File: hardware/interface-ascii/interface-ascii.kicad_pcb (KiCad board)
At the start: 2 copper layers, 88.9 x 119.4 mm, 51 parts, among them J1 Apple 2, J2 Apple 1, J3 UART, J4 Conn_01x05, J5 ISP header, J6 Keyboard, SW1 Options, U1 ATmega328P, U2 74LS166, U3 74LS138, U4 74LS138, U5 74LS07

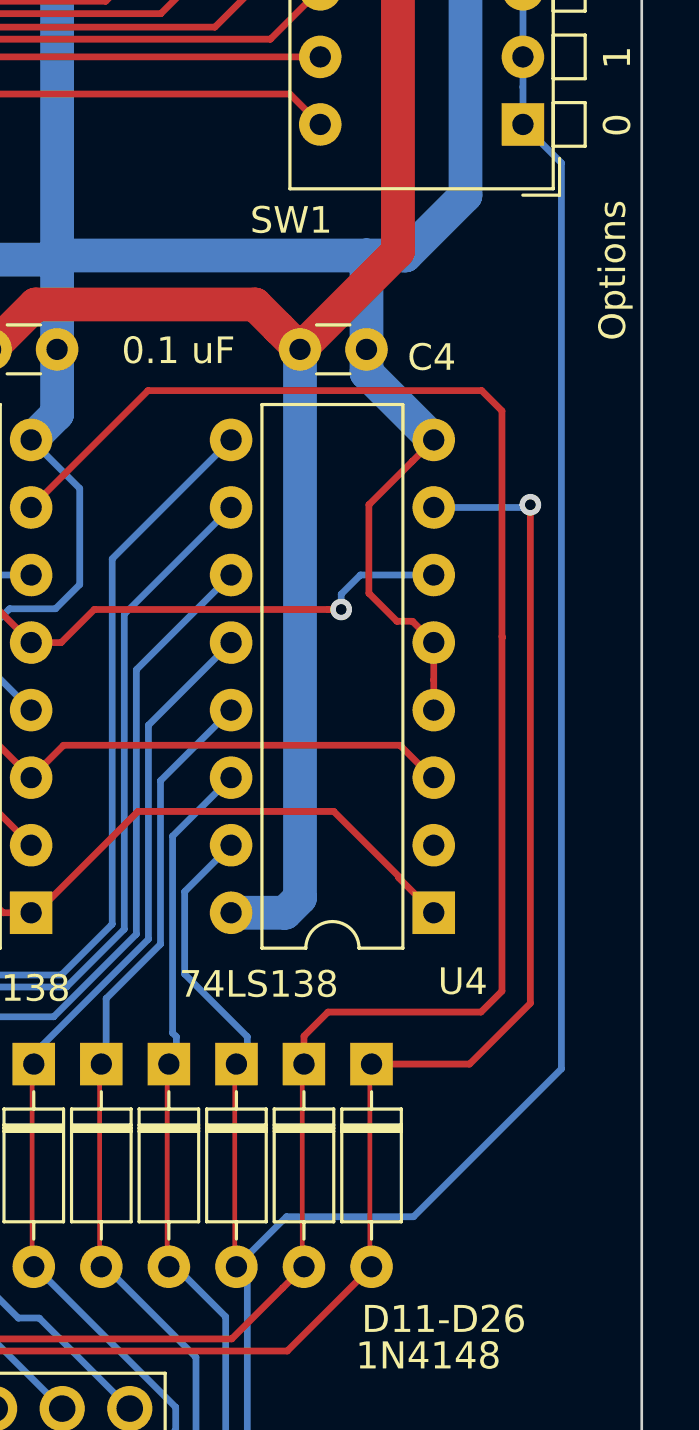
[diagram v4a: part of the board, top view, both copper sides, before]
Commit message: Move DIP switch to row 15
So keyboards with more than 8 rows can have keys on contiguous row numbers.
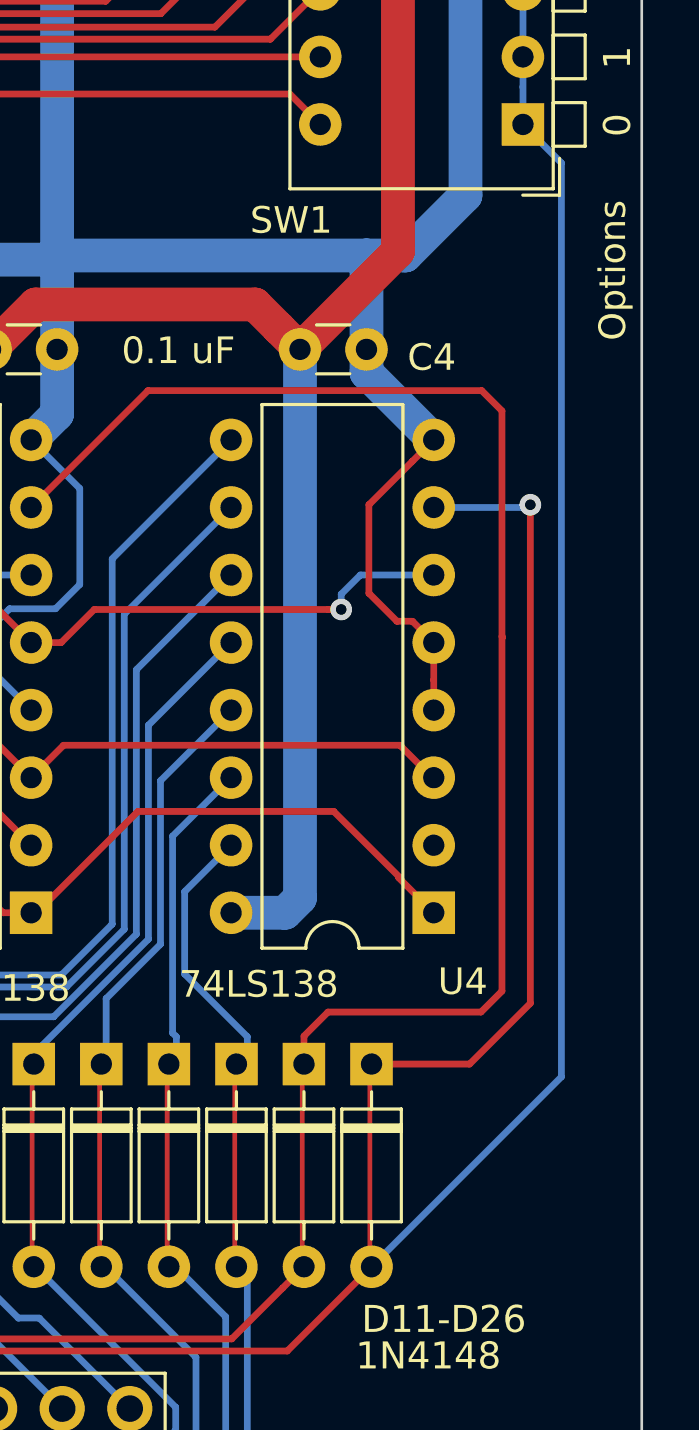
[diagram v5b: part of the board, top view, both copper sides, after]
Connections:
- SW1 pad 1: /Row8 -> /Row15
- SW1 pad 2: /Row8 -> /Row15
- SW1 pad 3: /Row8 -> /Row15
- SW1 pad 4: /Row8 -> /Row15
- SW1 pad 5: /Row8 -> /Row15
- SW1 pad 6: /Row8 -> /Row15
- SW1 pad 7: /Row8 -> /Row15
- SW1 pad 8: /Row8 -> /Row15
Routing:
- net /Row8: track 92.5 -> 23.3 mm
- net /Row15: track 18.9 -> 83.2 mm
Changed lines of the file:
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@@
     (thickness 1.6)
     (drawings 33)
-    (tracks 962)
+    (tracks 960)
     (zones 0)
     (modules 51)
@@
     )
     (pad 1 thru_hole rect (at 0 0 180) (size 1.6 1.6) (drill 0.8) (layers *.Cu *.Mask)
-      (net 37 /Row8))
+      (net 38 /Row15))
     (pad 9 thru_hole oval (at 7.62 17.78 180) (size 1.6 1.6) (drill 0.8) (layers *.Cu *.Mask)
       (net 73 "Net-(D27-Pad1)"))
     (pad 2 thru_hole oval (at 0 2.54 180) (size 1.6 1.6) (drill 0.8) (layers *.Cu *.Mask)
-      (net 37 /Row8))
+      (net 38 /Row15))
     (pad 10 thru_hole oval (at 7.62 15.24 180) (size 1.6 1.6) (drill 0.8) (layers *.Cu *.Mask)
       (net 56 "Net-(D20-Pad1)"))
     (pad 3 thru_hole oval (at 0 5.08 180) (size 1.6 1.6) (drill 0.8) (layers *.Cu *.Mask)
-      (net 37 /Row8))
+      (net 38 /Row15))
     (pad 11 thru_hole oval (at 7.62 12.7 180) (size 1.6 1.6) (drill 0.8) (layers *.Cu *.Mask)
       (net 59 "Net-(D26-Pad1)"))
     (pad 4 thru_hole oval (at 0 7.62 180) (size 1.6 1.6) (drill 0.8) (layers *.Cu *.Mask)
-      (net 37 /Row8))
+      (net 38 /Row15))
     (pad 12 thru_hole oval (at 7.62 10.16 180) (size 1.6 1.6) (drill 0.8) (layers *.Cu *.Mask)
       (net 55 "Net-(D19-Pad1)"))
     (pad 5 thru_hole oval (at 0 10.16 180) (size 1.6 1.6) (drill 0.8) (layers *.Cu *.Mask)
-      (net 37 /Row8))
+      (net 38 /Row15))
     (pad 13 thru_hole oval (at 7.62 7.62 180) (size 1.6 1.6) (drill 0.8) (layers *.Cu *.Mask)
       (net 58 "Net-(D25-Pad1)"))
     (pad 6 thru_hole oval (at 0 12.7 180) (size 1.6 1.6) (drill 0.8) (layers *.Cu *.Mask)
-      (net 37 /Row8))
+      (net 38 /Row15))
     (pad 14 thru_hole oval (at 7.62 5.08 180) (size 1.6 1.6) (drill 0.8) (layers *.Cu *.Mask)
       (net 54 "Net-(D18-Pad1)"))
     (pad 7 thru_hole oval (at 0 15.24 180) (size 1.6 1.6) (drill 0.8) (layers *.Cu *.Mask)
-      (net 37 /Row8))
+      (net 38 /Row15))
     (pad 15 thru_hole oval (at 7.62 2.54 180) (size 1.6 1.6) (drill 0.8) (layers *.Cu *.Mask)
       (net 57 "Net-(D24-Pad1)"))
     (pad 8 thru_hole oval (at 0 17.78 180) (size 1.6 1.6) (drill 0.8) (layers *.Cu *.Mask)
-      (net 37 /Row8))
+      (net 38 /Row15))
     (pad 16 thru_hole oval (at 7.62 0 180) (size 1.6 1.6) (drill 0.8) (layers *.Cu *.Mask)
       (net 53 "Net-(D17-Pad1)"))
@@
   (segment (start 237.086 169.572) (end 237.086 176.7856) (width 0.254) (layer B.Cu) (net 36))
   (segment (start 235.2318 167.7178) (end 237.086 169.572) (width 0.254) (layer B.Cu) (net 36))
-  (segment (start 248.262 110.63237) (end 248.262 112.041) (width 0.254) (layer B.Cu) (net 37))
-  (segment (start 248.262 109.501) (end 248.262 110.63237) (width 0.254) (layer B.Cu) (net 37))
-  (segment (start 248.262 112.041) (end 248.262 114.581) (width 0.254) (layer B.Cu) (net 37))
-  (segment (start 248.262 115.71237) (end 248.262 117.121) (width 0.254) (layer B.Cu) (net 37))
-  (segment (start 248.262 114.581) (end 248.262 115.71237) (width 0.254) (layer B.Cu) (net 37))
-  (segment (start 248.262 118.25237) (end 248.262 119.661) (width 0.254) (layer B.Cu) (net 37))
-  (segment (start 248.262 117.121) (end 248.262 118.25237) (width 0.254) (layer B.Cu) (net 37))
-  (segment (start 248.262 119.661) (end 248.262 122.201) (width 0.254) (layer B.Cu) (net 37))
-  (segment (start 248.262 123.33237) (end 248.262 124.741) (width 0.254) (layer B.Cu) (net 37))
-  (segment (start 248.262 122.201) (end 248.262 123.33237) (width 0.254) (layer B.Cu) (net 37))
   (segment (start 236.47959 178.56041) (end 228.85321 178.56041) (width 0.254) (layer B.Cu) (net 37))
   (segment (start 228.85321 178.56041) (end 225.8592 175.5664) (width 0.254) (layer B.Cu) (net 37))
   (segment (start 237.8988 177.1412) (end 236.47959 178.56041) (width 0.254) (layer B.Cu) (net 37))
   (segment (start 237.8988 167.7178) (end 237.8988 177.1412) (width 0.254) (layer B.Cu) (net 37))
-  (segment (start 239.3696 165.8128) (end 237.49 167.6924) (width 0.254) (layer B.Cu) (net 37))
-  (segment (start 244.1472 165.8128) (end 239.3696 165.8128) (width 0.254) (layer B.Cu) (net 37))
-  (segment (start 249.7098 126.1888) (end 249.7098 160.2502) (width 0.254) (layer B.Cu) (net 37))
-  (segment (start 249.7098 160.2502) (end 244.1472 165.8128) (width 0.254) (layer B.Cu) (net 37))
-  (segment (start 248.262 124.741) (end 249.7098 126.1888) (width 0.254) (layer B.Cu) (net 37))
-  (segment (start 248.262 108.09237) (end 248.262 109.501) (width 0.254) (layer B.Cu) (net 37))
-  (segment (start 248.262 106.961) (end 248.262 108.09237) (width 0.254) (layer B.Cu) (net 37))
   (segment (start 242.57 167.6924) (end 239.401378 170.861022) (width 0.254) (layer F.Cu) (net 38))
   (segment (start 226.709199 172.176401) (end 225.8592 173.0264) (width 0.254) (layer F.Cu) (net 38))
   (segment (start 239.401378 170.861022) (end 228.024578 170.861022) (width 0.254) (layer F.Cu) (net 38))
   (segment (start 228.024578 170.861022) (end 226.709199 172.176401) (width 0.254) (layer F.Cu) (net 38))
+  (segment (start 248.262 106.961) (end 248.262 108.09237) (width 0.254) (layer B.Cu) (net 38))
+  (segment (start 248.262 108.09237) (end 248.262 109.501) (width 0.254) (layer B.Cu) (net 38))
+  (segment (start 248.262 122.201) (end 248.262 123.33237) (width 0.254) (layer B.Cu) (net 38))
+  (segment (start 248.262 123.33237) (end 248.262 124.741) (width 0.254) (layer B.Cu) (net 38))
+  (segment (start 248.262 119.661) (end 248.262 122.201) (width 0.254) (layer B.Cu) (net 38))
+  (segment (start 248.262 117.121) (end 248.262 118.25237) (width 0.254) (layer B.Cu) (net 38))
+  (segment (start 248.262 118.25237) (end 248.262 119.661) (width 0.254) (layer B.Cu) (net 38))
+  (segment (start 248.262 114.581) (end 248.262 115.71237) (width 0.254) (layer B.Cu) (net 38))
+  (segment (start 248.262 115.71237) (end 248.262 117.121) (width 0.254) (layer B.Cu) (net 38))
+  (segment (start 248.262 112.041) (end 248.262 114.581) (width 0.254) (layer B.Cu) (net 38))
+  (segment (start 248.262 109.501) (end 248.262 110.63237) (width 0.254) (layer B.Cu) (net 38))
+  (segment (start 248.262 110.63237) (end 248.262 112.041) (width 0.254) (layer B.Cu) (net 38))
+  (segment (start 249.7098 160.5526) (end 242.57 167.6924) (width 0.254) (layer B.Cu) (net 38))
+  (segment (start 249.7098 126.1888) (end 249.7098 160.5526) (width 0.254) (layer B.Cu) (net 38))
+  (segment (start 248.262 124.741) (end 249.7098 126.1888) (width 0.254) (layer B.Cu) (net 38))
   (segment (start 224.7416 170.2578) (end 225.6306 170.2578) (width 0.254) (layer B.Cu) (net 39))
   (segment (start 227.549201 172.176401) (end 228.3992 173.0264) (width 0.254) (layer B.Cu) (net 39))

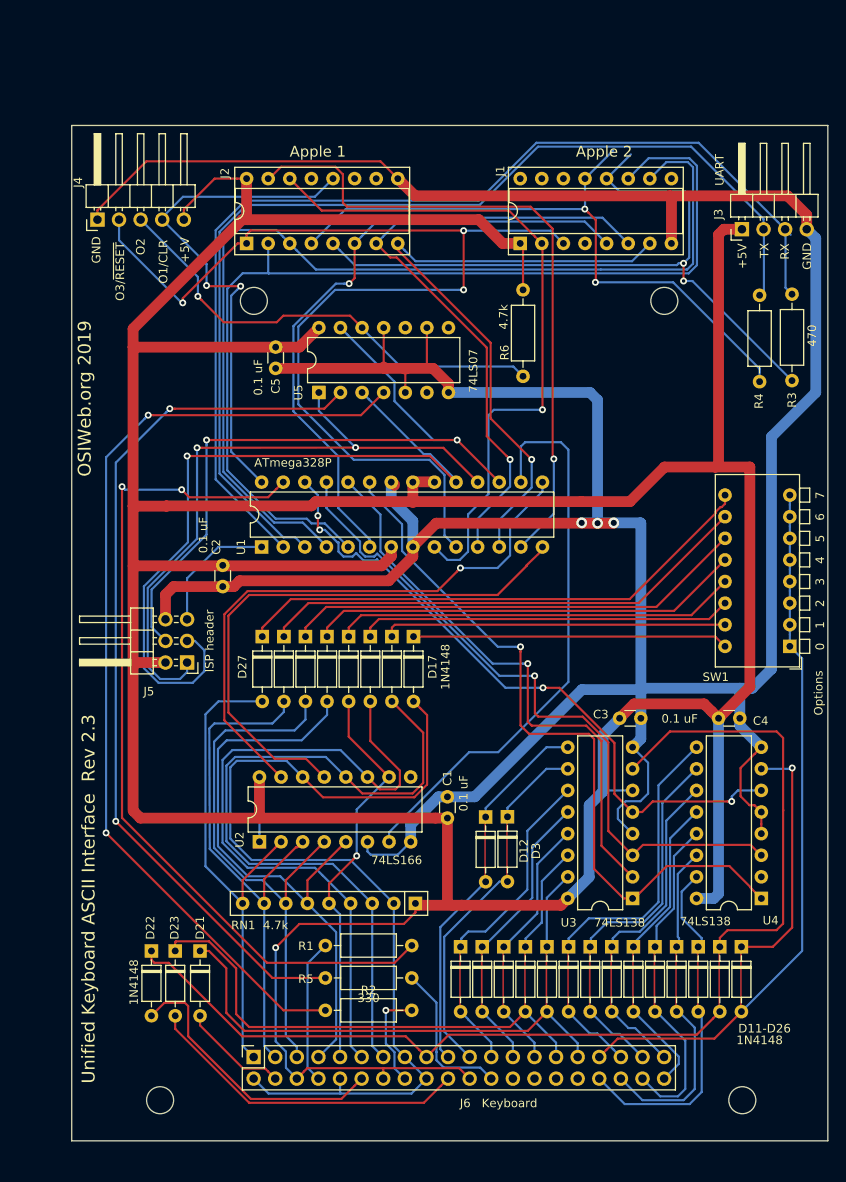
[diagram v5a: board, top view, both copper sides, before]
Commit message: Add SOL-20 connector
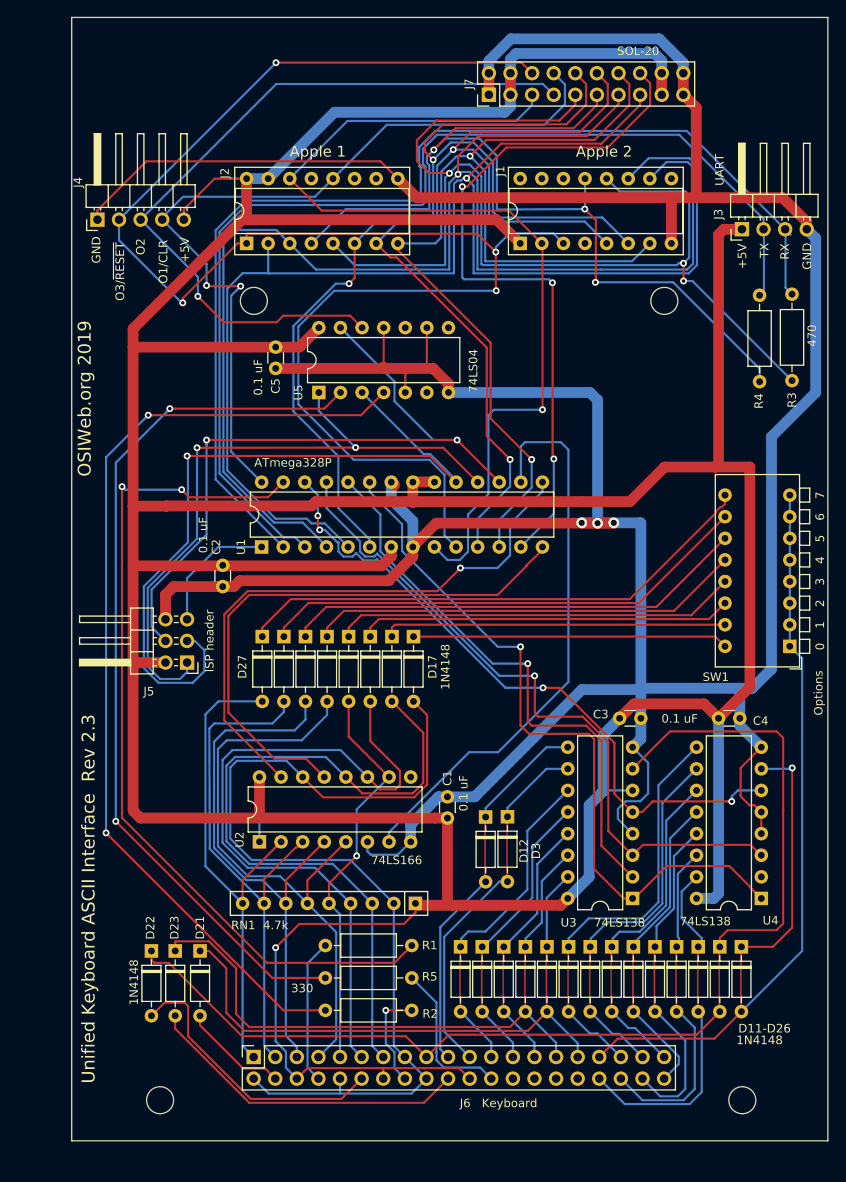
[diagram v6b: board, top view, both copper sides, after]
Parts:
- removed R6: 4.7k, Resistor_THT:R_Axial_DIN0207_L6.3mm_D2.5mm_P10.16mm_Horizontal
- added J7: SOL-20, unikbd:SOL20-header-vertical, F.Cu at (212.9, 59.9)
- U5: value 74LS07 -> 74LS04
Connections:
- J2 pad 15: /D7 -> +5V
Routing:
- net /OUT3: track 130.1 -> 190.1 mm, vias 3 -> 4
- net +5V: track 528.6 -> 586.0 mm
- net /D3: track 120.3 -> 167.0 mm, vias 0 -> 1
- net /D2: track 118.9 -> 165.1 mm, vias 0 -> 1
- net /D0: track 84.9 -> 131.1 mm, vias 2 -> 3
- net /D6: track 75.1 -> 119.8 mm, vias 1 -> 2
- net GND: track 414.7 -> 459.3 mm
- net /D4: track 77.9 -> 120.1 mm, vias 1 -> 2
- net /D5: track 73.4 -> 112.4 mm, vias 1 -> 2
- net /OUT1: track 61.6 -> 96.7 mm
- net /OUT2: track 54.6 -> 89.0 mm
- net /~STROBE: track 81.3 -> 114.5 mm
- net /D1: track 76.3 -> 108.7 mm, vias 2 -> 3
- net /D7: track 77.9 -> 84.6 mm, vias 1 -> 3
- net /Tx: track 123.4 -> 128.6 mm
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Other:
- board size 88.9 x 119.4 mm -> 88.9 x 132.1 mm
